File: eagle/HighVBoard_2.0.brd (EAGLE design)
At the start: 113 x 45.7 mm, 25 parts, among them IC2 K155D1, IC3 K155D1, IC4 K155D1, IC5 K155D1, T1 INS-3, T2 IN-8, T3 IN-8, T4 IN-8, T5 IN-8

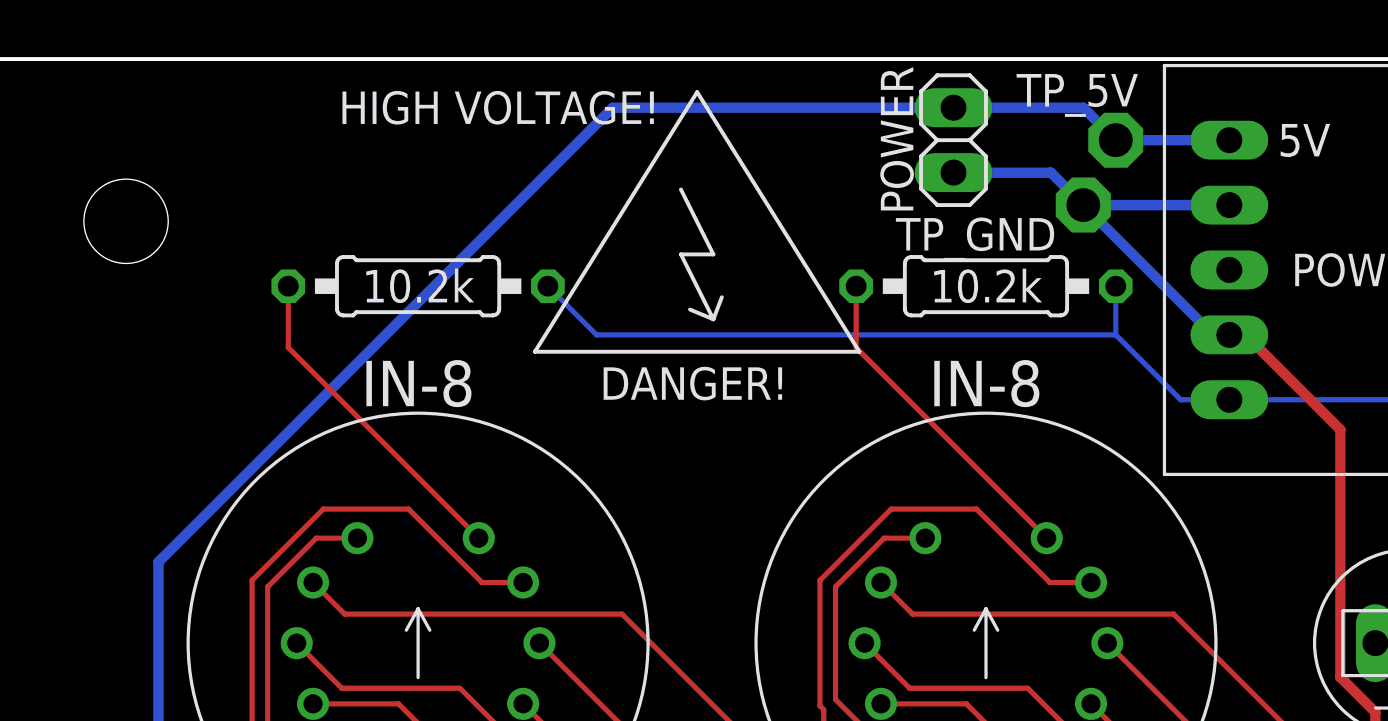
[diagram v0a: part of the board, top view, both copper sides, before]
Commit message: added clearance for wodden board in front of switches and jack
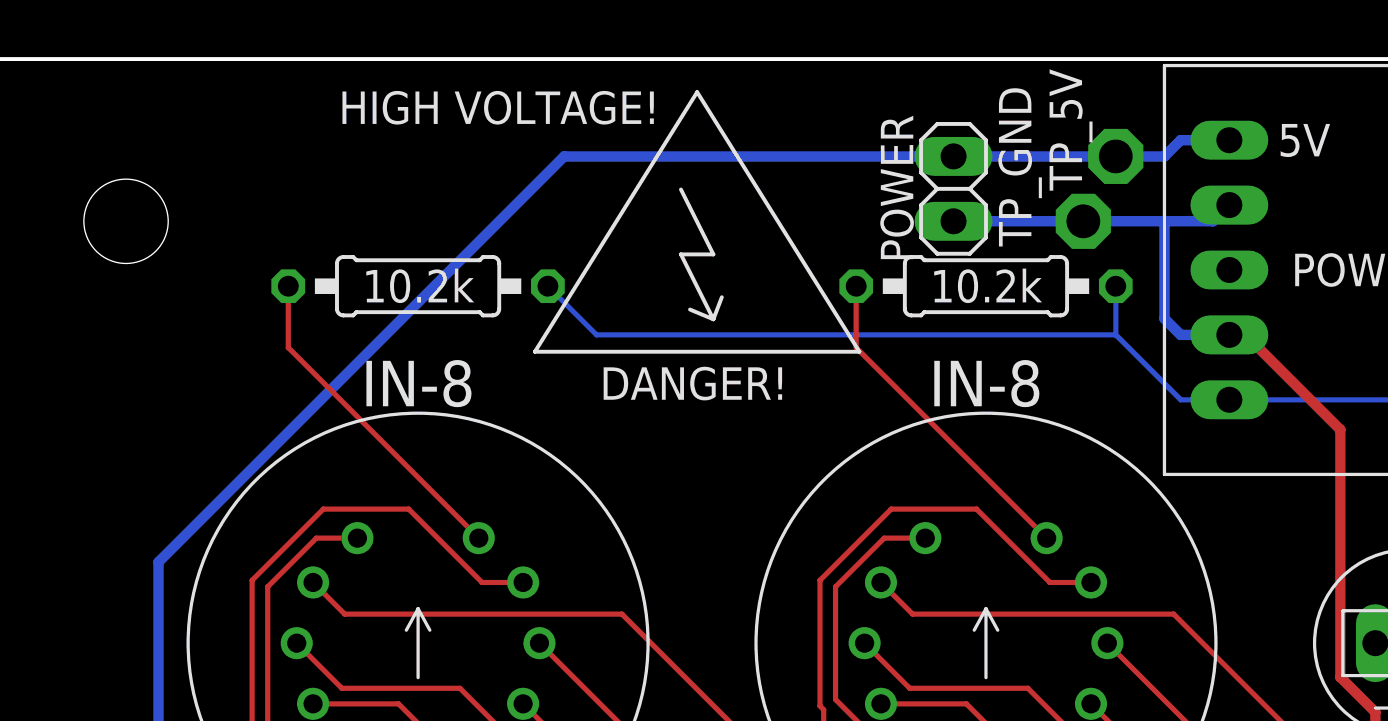
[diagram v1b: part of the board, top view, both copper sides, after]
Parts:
- moved POWER 1.91 mm to (38.7, 40.6)
- moved TP_5V 0.64 mm to (45.1, 41.9)
- moved TP_GND 0.64 mm to (43.8, 39.4)
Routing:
- net GND: track 157.7 -> 156.2 mm
- net +5V: track 176.0 -> 174.9 mm
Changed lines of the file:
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@@
 <dimension x1="95.25" y1="31.75" x2="95.25" y2="45.72" x3="124.46" y3="38.735" textsize="1.27" layer="47"/>
 <dimension x1="38.735" y1="43.815" x2="0" y2="43.815" x3="19.3675" y3="47.625" textsize="1.27" layer="47"/>
-<dimension x1="38.735" y1="45.72" x2="38.735" y2="43.815" x3="-1.905" y3="44.7675" textsize="1.27" layer="47"/>
 <dimension x1="6.35" y1="6.35" x2="6.35" y2="0" x3="6.35" y3="0" textsize="1.778" layer="47" dtype="diameter"/>
 <dimension x1="6.35" y1="6.35" x2="0" y2="6.35" x3="0" y3="6.35" textsize="1.778" layer="47" dtype="diameter"/>
@@
 <dimension x1="106.68" y1="6.35" x2="106.68" y2="0" x3="106.68" y3="0" textsize="1.778" layer="47" dtype="diameter"/>
 <dimension x1="106.68" y1="6.35" x2="113.03" y2="6.35" x3="113.03" y3="6.35" textsize="1.778" layer="47" dtype="diameter"/>
+<dimension x1="38.735" y1="41.91" x2="38.735" y2="45.72" x3="-11.43" y3="43.815" textsize="1.778" layer="47"/>
 </plain>
 <attributes>
@@
 <attribute name="VALUE" x="67.945" y="40.005" size="0.0254" layer="27"/>
 </element>
-<element name="TP_5V" library="testpad" library_urn="urn:adsk.eagle:library:385" package="P1-13" package3d_urn="urn:adsk.eagle:package:27946/1" value="TPPAD1-13" x="45.085" y="42.545" smashed="yes">
-<attribute name="NAME" x="43.5864" y="44.5008" size="1.27" layer="25" font="vector" align="center"/>
-<attribute name="TP_SIGNAL_NAME" value="" x="43.815" y="40.005" size="1" layer="37"/>
-<attribute name="VALUE" x="45.085" y="41.275" size="0.0254" layer="27"/>
-</element>
-<element name="TP_GND" library="testpad" library_urn="urn:adsk.eagle:library:385" package="P1-13" package3d_urn="urn:adsk.eagle:package:27946/1" value="TPPAD1-13" x="43.815" y="40.005" smashed="yes">
-<attribute name="NAME" x="39.624" y="38.862" size="1.27" layer="25" font="vector" align="center"/>
-<attribute name="TP_SIGNAL_NAME" value="" x="42.545" y="37.465" size="1" layer="37"/>
-<attribute name="VALUE" x="43.815" y="38.735" size="0.0254" layer="27"/>
-</element>
-<element name="POWER" library="pinhead" library_urn="urn:adsk.eagle:library:325" package="1X02" package3d_urn="urn:adsk.eagle:package:22435/2" value="" x="38.735" y="42.545" smashed="yes" rot="R270">
-<attribute name="NAME" x="36.5252" y="42.545" size="1.27" layer="25" font="vector" rot="R270" align="center"/>
-<attribute name="VALUE" x="35.56" y="45.085" size="1.27" layer="27" rot="R270"/>
+<element name="TP_5V" library="testpad" library_urn="urn:adsk.eagle:library:385" package="P1-13" package3d_urn="urn:adsk.eagle:package:27946/1" value="TPPAD1-13" x="45.085" y="41.91" smashed="yes">
+<attribute name="NAME" x="43.1292" y="42.9514" size="1.27" layer="25" font="vector" rot="R90" align="center"/>
+<attribute name="TP_SIGNAL_NAME" value="" x="43.815" y="39.37" size="1" layer="37"/>
+<attribute name="VALUE" x="45.085" y="40.64" size="0.0254" layer="27"/>
+</element>
+<element name="TP_GND" library="testpad" library_urn="urn:adsk.eagle:library:385" package="P1-13" package3d_urn="urn:adsk.eagle:package:27946/1" value="TPPAD1-13" x="43.815" y="39.37" smashed="yes">
+<attribute name="NAME" x="41.148" y="41.529" size="1.27" layer="25" font="vector" rot="R90" align="center"/>
+<attribute name="TP_SIGNAL_NAME" value="" x="42.545" y="36.83" size="1" layer="37"/>
+<attribute name="VALUE" x="43.815" y="38.1" size="0.0254" layer="27"/>
+</element>
+<element name="POWER" library="pinhead" library_urn="urn:adsk.eagle:library:325" package="1X02" package3d_urn="urn:adsk.eagle:package:22435/2" value="" x="38.735" y="40.64" smashed="yes" rot="R270">
+<attribute name="NAME" x="36.5252" y="40.64" size="1.27" layer="25" font="vector" rot="R270" align="center"/>
+<attribute name="VALUE" x="35.56" y="43.18" size="1.27" layer="27" rot="R270"/>
 </element>
 <element name="U$2" library="Nixie" package="NIXIE-PSU" value="NIXIE-PSU" x="49.53" y="37.465" smashed="yes" rot="R270"/>
@@
 <contactref element="TP_GND" pad="TP"/>
 <contactref element="POWER" pad="2"/>
-<wire x1="43.815" y1="40.005" x2="42.545" y2="41.275" width="0.4064" layer="16"/>
-<wire x1="38.735" y1="41.275" x2="42.545" y2="41.275" width="0.4064" layer="16"/>
+<wire x1="43.815" y1="39.37" x2="38.735" y2="39.37" width="0.4064" layer="16"/>
 <wire x1="22.225" y1="15.875" x2="22.225" y2="12.0396" width="0.4064" layer="16"/>
 <wire x1="22.225" y1="12.0396" x2="43.815" y2="12.0396" width="0.4064" layer="16"/>
@@
 <contactref element="U$2" pad="2"/>
 <contactref element="U$2" pad="4"/>
-<wire x1="49.53" y1="40.005" x2="43.815" y2="40.005" width="0.4064" layer="16"/>
-<wire x1="49.53" y1="34.925" x2="48.895" y2="34.925" width="0.4064" layer="16"/>
-<wire x1="48.895" y1="34.925" x2="43.815" y2="40.005" width="0.4064" layer="16"/>
+<wire x1="49.53" y1="40.005" x2="48.895" y2="39.37" width="0.4064" layer="16"/>
+<wire x1="48.895" y1="39.37" x2="46.99" y2="39.37" width="0.4064" layer="16"/>
 <contactref element="U$1" pad="3"/>
 <contactref element="C1" pad="2"/>
 <contactref element="C3" pad="2"/>
+<wire x1="46.99" y1="39.37" x2="43.815" y2="39.37" width="0.4064" layer="16"/>
 <wire x1="54.61" y1="12.0396" x2="54.61" y2="13.0048" width="0.4064" layer="16"/>
 <wire x1="58.42" y1="13.0048" x2="58.42" y2="12.0396" width="0.4064" layer="16"/>
@@
 <wire x1="55.245" y1="16.9164" x2="55.245" y2="13.6398" width="0.4064" layer="1"/>
 <wire x1="55.245" y1="13.6398" x2="54.61" y2="13.0048" width="0.4064" layer="1"/>
+<wire x1="49.53" y1="34.925" x2="47.625" y2="34.925" width="0.4064" layer="16"/>
+<wire x1="47.625" y1="34.925" x2="46.99" y2="35.56" width="0.4064" layer="16"/>
+<wire x1="46.99" y1="35.56" x2="46.99" y2="39.37" width="0.4064" layer="16"/>
 </signal>
 <signal name="N$7" class="3">
@@
 <contactref element="TP_5V" pad="TP"/>
 <contactref element="POWER" pad="1"/>
-<wire x1="45.085" y1="42.545" x2="43.815" y2="43.815" width="0.4064" layer="16"/>
-<wire x1="43.815" y1="43.815" x2="38.735" y2="43.815" width="0.4064" layer="16"/>
+<wire x1="45.085" y1="41.91" x2="38.735" y2="41.91" width="0.4064" layer="16"/>
 <wire x1="22.225" y1="8.255" x2="22.225" y2="11.43" width="0.4064" layer="16"/>
 <wire x1="22.225" y1="11.43" x2="43.815" y2="11.43" width="0.4064" layer="16"/>
@@
 <wire x1="71.755" y1="11.43" x2="93.345" y2="11.43" width="0.4064" layer="16"/>
 <wire x1="93.345" y1="11.43" x2="93.345" y2="8.255" width="0.4064" layer="16"/>
-<wire x1="38.735" y1="43.815" x2="25.4" y2="43.815" width="0.4064" layer="16"/>
+<wire x1="38.735" y1="41.91" x2="23.495" y2="41.91" width="0.4064" layer="16"/>
 <contactref element="U$2" pad="1"/>
-<wire x1="49.53" y1="42.545" x2="45.085" y2="42.545" width="0.4064" layer="16"/>
+<wire x1="49.53" y1="42.545" x2="47.625" y2="42.545" width="0.4064" layer="16"/>
+<wire x1="47.625" y1="42.545" x2="46.99" y2="41.91" width="0.4064" layer="16"/>
+<wire x1="46.99" y1="41.91" x2="45.085" y2="41.91" width="0.4064" layer="16"/>
 <contactref element="C1" pad="1"/>
 <contactref element="C3" pad="1"/>
@@
 <wire x1="9.525" y1="11.43" x2="8.89" y2="10.795" width="0.4064" layer="16"/>
 <wire x1="22.225" y1="11.43" x2="9.525" y2="11.43" width="0.4064" layer="16"/>
-<wire x1="25.4" y1="43.815" x2="7.62" y2="26.035" width="0.4064" layer="16"/>
+<wire x1="23.495" y1="41.91" x2="7.62" y2="26.035" width="0.4064" layer="16"/>
 <wire x1="7.62" y1="12.065" x2="8.89" y2="10.795" width="0.4064" layer="16"/>
 <wire x1="7.62" y1="26.035" x2="7.62" y2="12.065" width="0.4064" layer="16"/>
